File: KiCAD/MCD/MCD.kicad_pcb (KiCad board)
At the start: 2 copper layers, 196.3 x 114.9 mm, 76 parts, among them J1 DBUS_LOW, J2 DBUS_HIGH, J3 ABUS, J4 POWER, J5 JTAG, J6 Conn_01x02_Male, J7 DUART A, J8 DUART B, SW1 SW_Push, U1 XC9572XL-10VQG44C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

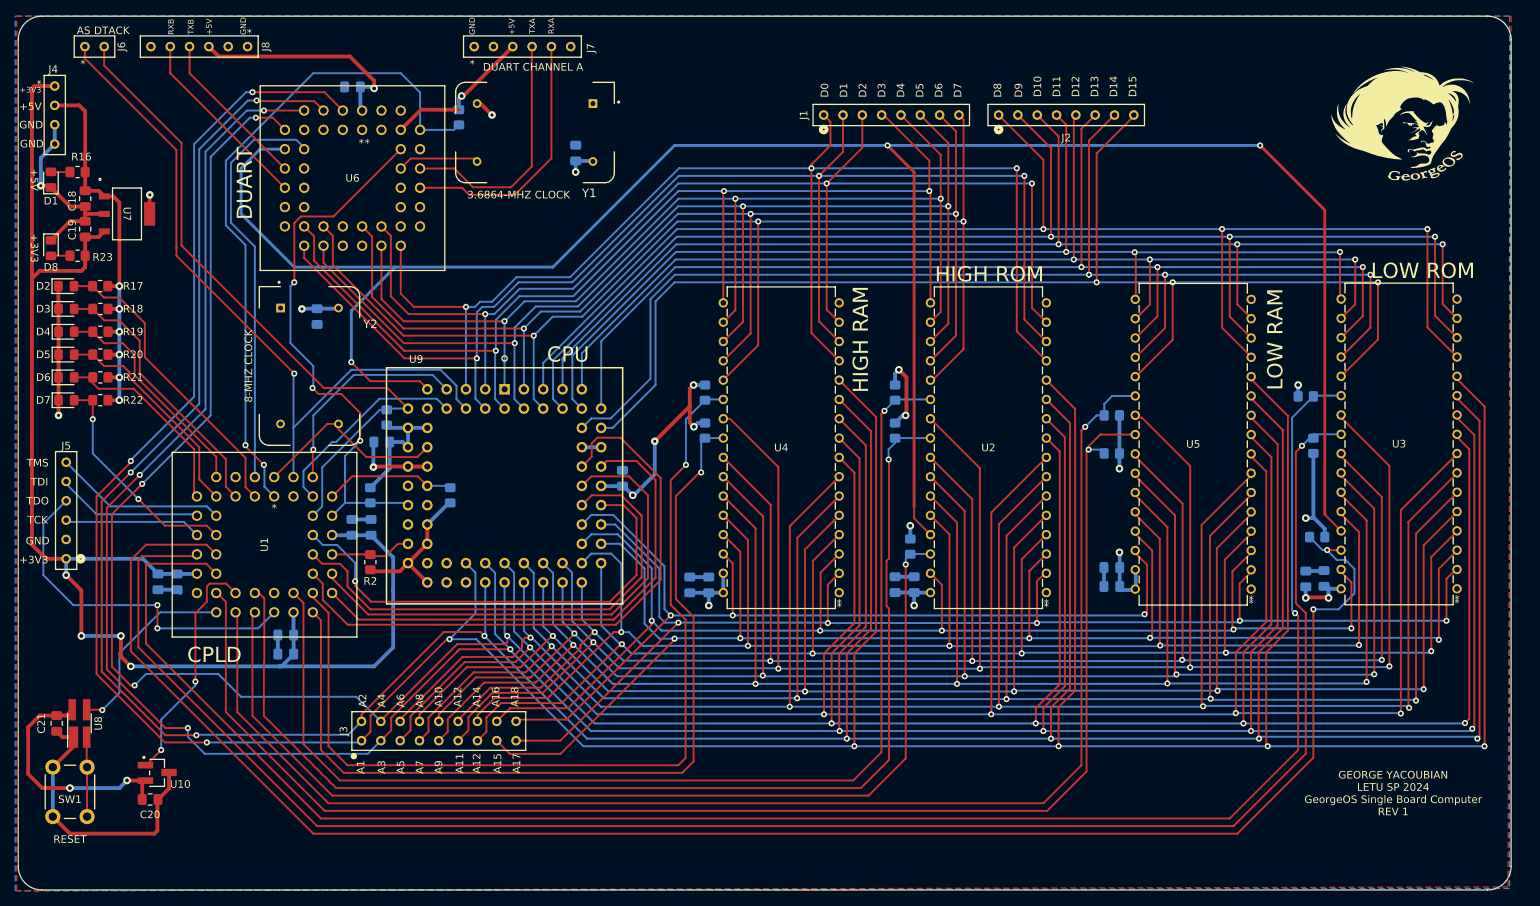
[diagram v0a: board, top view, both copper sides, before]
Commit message: changed xc9572xl schematic symbol from vq44 to pc44
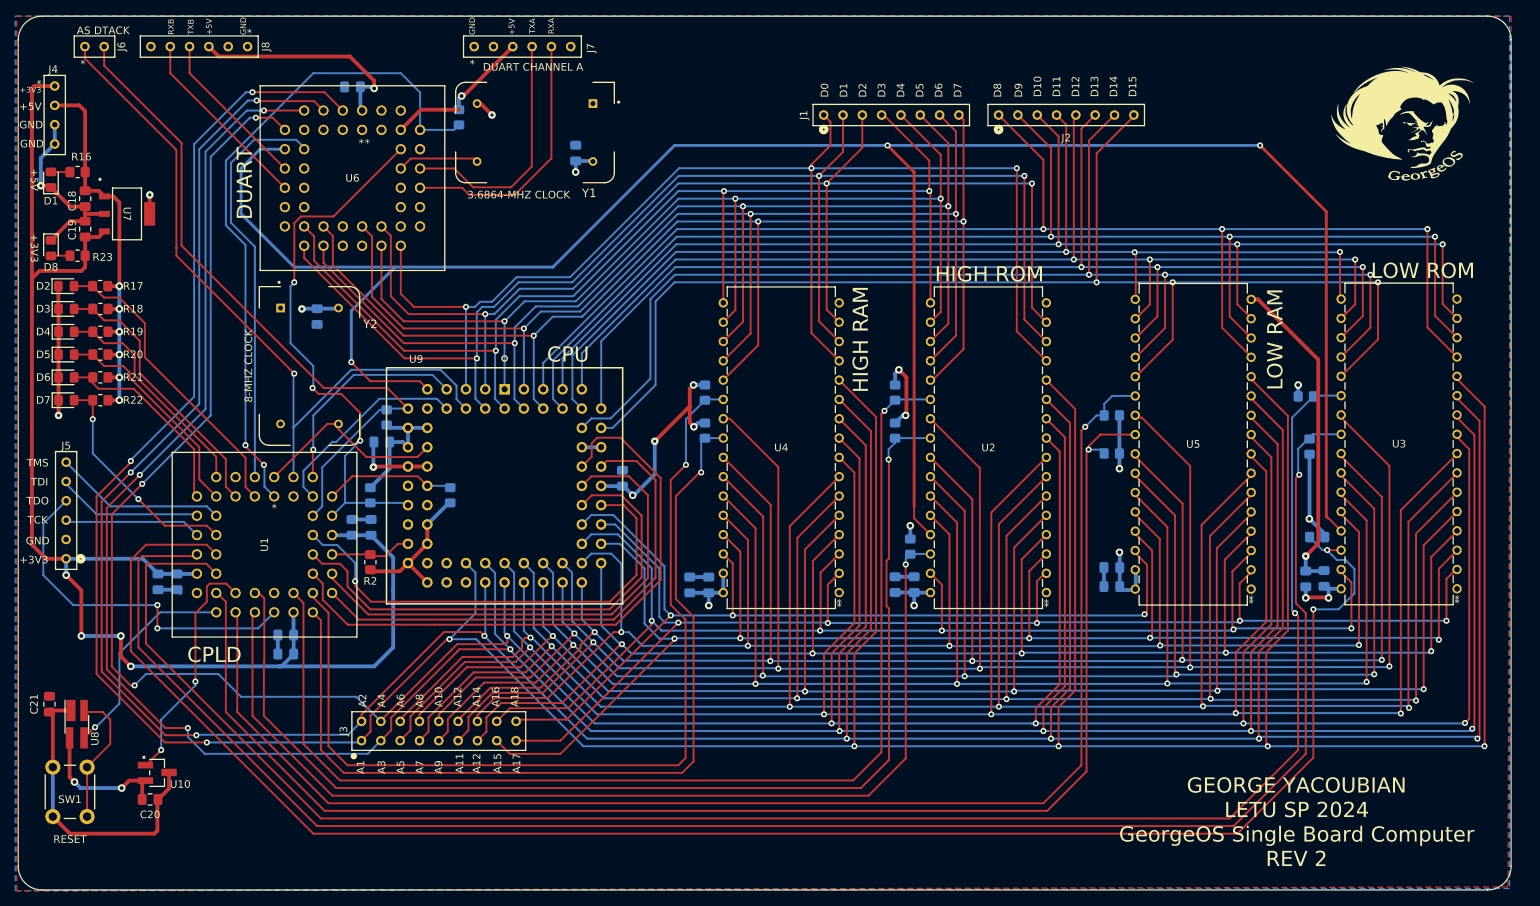
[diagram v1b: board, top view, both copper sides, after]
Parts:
- U8: footprint Package_TO_SOT_SMD:SOT-143_Handsoldering -> Package_TO_SOT_SMD:SOT-143R_Reverse_Handsoldering
- moved C21 2.71 mm to (104.8, 162.0)
- moved R14 0.51 mm to (270.5, 128.1)
- moved U8 0.36 mm to (108.4, 164.6), turned to -90 degrees
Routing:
- net GND: track 117.1 -> 159.9 mm, vias 5 -> 6
- net +5V: track 277.0 -> 262.6 mm
- net /SW_IN: track 10.4 -> 18.0 mm
- net BRESET: track 25.5 -> 28.1 mm
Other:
- board text added: "GEORGE YACOUBIAN LETU SP 2024 GeorgeOS Single Board Computer REV 2"
- board text removed: "GEORGE YACOUBIAN LETU SP 2024 GeorgeOS Single Board Computer REV 1"

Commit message: finished pcb, not checked yet but drc is good
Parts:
- R2: moved to B.Cu
- U1: value XC9572XL-10VQG44C -> XC9572XL-PC44
- moved C6 12.6 mm to (135.8, 142.8)
- moved C14 11.9 mm to (130.6, 142.8), turned to 0 degrees
- moved C9 11.3 mm to (135.8, 139.5), turned to 180 degrees
- moved J5 10.5 mm to (107.5, 147.0)
- moved C12 8.97 mm to (130.5, 145.0), turned to 0 degrees
- moved C7 8.91 mm to (135.8, 137.2), turned to 180 degrees
- moved C5 7.88 mm to (135.8, 145.0)
- moved R2 2.48 mm to (149.2, 142.2)
- moved R9 2.25 mm to (149.2, 134.5)
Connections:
- U1 pad 1: DUARTCS -> AS
- U1 pad 10: TMS -> GND
- U1 pad 11: TCK -> RAMHCE2
- U1 pad 12: LED5 -> unconnected-(U1-Pad12)
- U1 pad 13: RAMHOE -> RAMHCE
- U1 pad 14: RAMHCE2 -> RAMHOE
- U1 pad 15: +3V3 -> TDI
- U1 pad 16: RAMHCE -> TMS
- U1 pad 17: GND -> TCK
- U1 pad 18: BRESET -> SRESET
- U1 pad 19: ROMHOE -> BRESET
- U1 pad 2: DUART_DTACK -> LED0
- U1 pad 20: ROMHCE -> ROMHOE
- U1 pad 21: SRESET -> +3V3
- U1 pad 22: RAMLCE2 -> ROMHCE
- U1 pad 23: RAMLOE -> GND
- U1 pad 24: TDO -> RAMLOE
- U1 pad 25: GND -> RAMLCE2
- U1 pad 26: +3V3 -> ROMLOE
- U1 pad 28: ROMLOE -> ROMLCE
- U1 pad 29: A22 -> A23
- U1 pad 3: LED0 -> DUARTCS
- U1 pad 30: ROMLCE -> TDO
- U1 pad 31: A21 -> GND
- U1 pad 32: A23 -> +3V3
- U1 pad 33: BERR -> A21
- U1 pad 34: A20 -> A22
- U1 pad 35: +3V3 -> A19
- U1 pad 36: A19 -> A20
- U1 pad 38: CPLD_DTACK -> BERR
- U1 pad 4: GND -> LED1
- U1 pad 40: UDS -> CPLD_DTACK
- U1 pad 41: LDS -> +3V3
- U1 pad 42: AS -> UDS
- U1 pad 43: unconnected-(U1-Pad43) -> LDS
- U1 pad 44: CLK -> DUART_DTACK
- U1 pad 5: LED1 -> LED2
- U1 pad 6: LED2 -> CLK
- U1 pad 9: TDI -> LED5
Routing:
- net +3V3: track 188.2 -> 174.1 mm, vias 4 -> 3
- net GND: track 159.9 -> 173.2 mm
- net TDO: track 46.9 -> 37.4 mm
- net CLK: track 25.8 -> 34.3 mm
- net SRESET: track 31.3 -> 24.0 mm
- net A22: track 67.6 -> 73.2 mm
- net CPLD_DTACK: track 90.4 -> 85.3 mm
- net A23: track 80.8 -> 76.0 mm
- net RAMLOE: track 152.2 -> 148.3 mm
- net AS: track 97.0 -> 100.7 mm, vias 1 -> 2
- net ROMHOE: track 188.9 -> 185.3 mm
- net BERR: track 10.7 -> 14.4 mm
- net +5V: track 262.6 -> 259.0 mm
- net LED5: track 30.1 -> 26.5 mm
- net LED2: track 29.7 -> 33.3 mm
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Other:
- board text added: "{dblquote}Therefore, if anyone is in Christ, he is a new creation. The old has passed away; behold, the new has come.{dblquote} - 2 Corinthians 5:17"

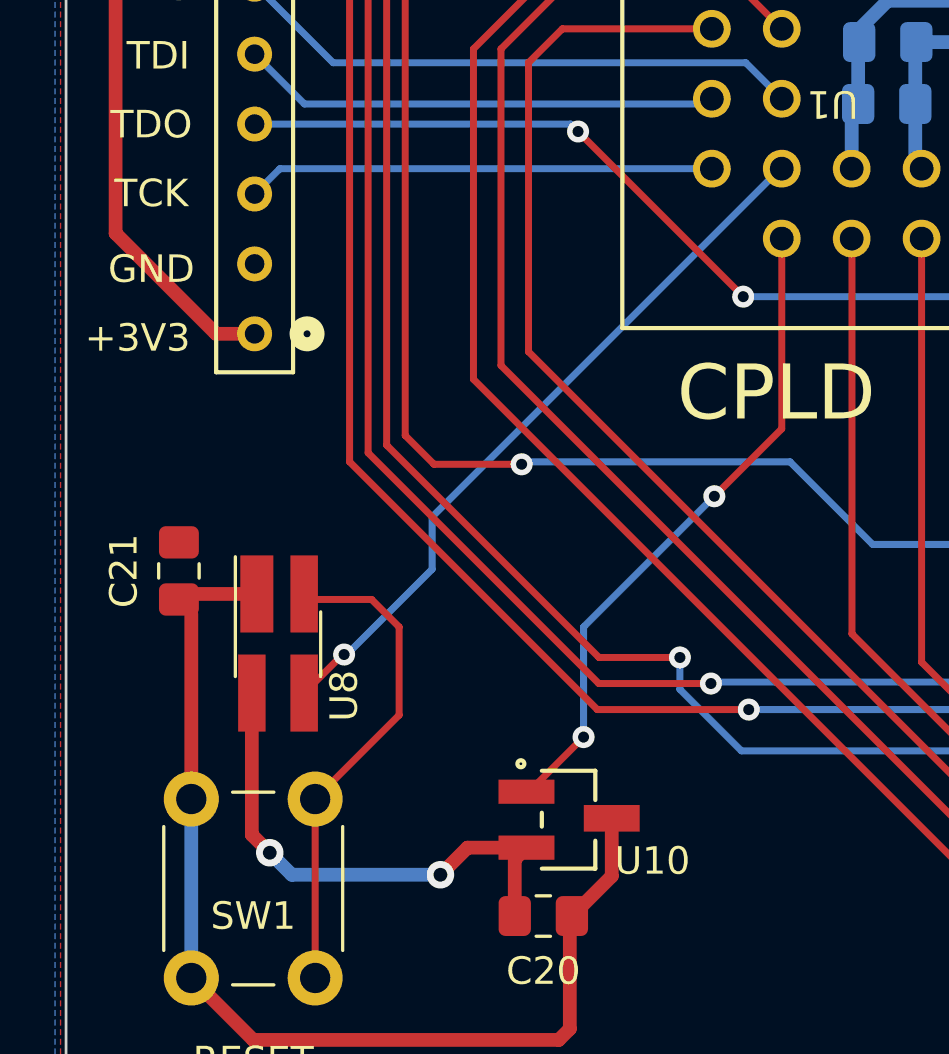
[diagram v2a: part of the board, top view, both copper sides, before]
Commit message: now converts to hex to bin and bin to hex
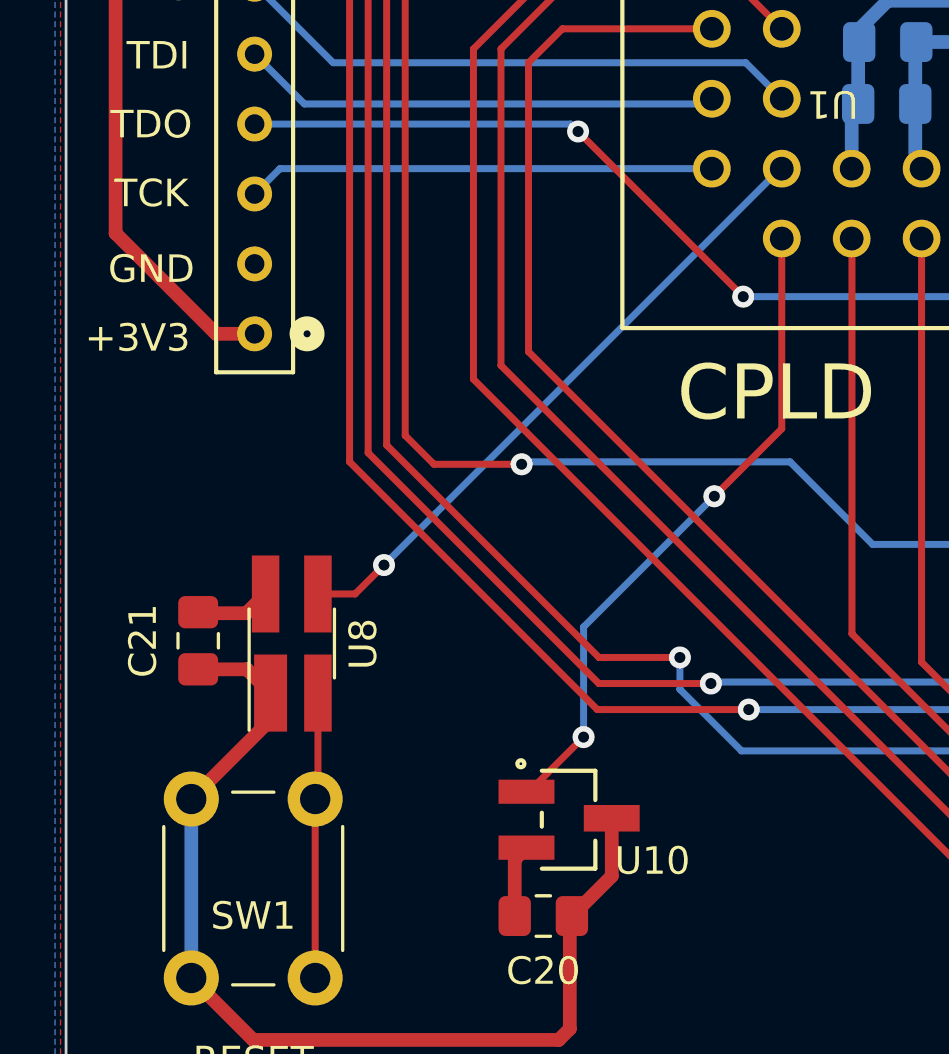
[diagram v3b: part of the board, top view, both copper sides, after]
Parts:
- U8: footprint Package_TO_SOT_SMD:SOT-143R_Reverse_Handsoldering -> Package_TO_SOT_SMD:SOT-143_Handsoldering
- moved C21 2.63 mm to (105.5, 164.5)
- moved U8 0.50 mm to (108.9, 164.6), turned to 90 degrees
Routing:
- net +5V: track 259.0 -> 245.6 mm, vias 27 -> 25
- net /SW_IN: track 18.0 -> 10.4 mm
- net BRESET: track 26.4 -> 23.2 mm
- net GND: track 173.2 -> 170.4 mm
